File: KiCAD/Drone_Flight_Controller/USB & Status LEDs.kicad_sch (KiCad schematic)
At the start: 26 parts, among them P601 USB_C_Plug_USB2.0, Q601 BC846C, Q602 BC846C, Q603 BC846C, Q604 BC846C, Q605 BC846C, Q606 BC846C, Q607 BC846C, U601 MCP2200-I-SO, Y601 CSTNE12M0GH5L000R0

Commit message: Change footprints to HandSoldering
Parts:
- D601: footprint Diode_SMD:D_SOD-323F -> Diode_SMD:D_SOD-323_HandSoldering
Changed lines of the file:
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@@
 			)
 		)
-		(property "Footprint" "Diode_SMD:D_SOD-323F"
+		(property "Footprint" "Diode_SMD:D_SOD-323_HandSoldering"
 			(at 97.79 45.72 0)
 			(effects

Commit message: add footprint of USB C connector
add footprint of USB C connector
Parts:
- P601: footprint Connector_PinHeader_2.54mm:PinHeader_1x07_P2.54mm_Vertical -> Connector_USB:USB_C_Receptacle_HRO_TYPE-C-31-M-12
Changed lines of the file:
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@@
 			)
 		)
-		(property "Footprint" "Connector_PinHeader_2.54mm:PinHeader_1x07_P2.54mm_Vertical"
+		(property "Footprint" "Connector_USB:USB_C_Receptacle_HRO_TYPE-C-31-M-12"
 			(at 80.01 60.96 0)
 			(effects

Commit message: part placement and routing
part placement and routing
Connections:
- net -BATT is gone; now on net GND: Q603.2 (E), Q604.2 (E), Q605.2 (E)
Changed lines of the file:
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@@
-	)
-	(symbol
-		(lib_id "power:-BATT")
-		(at 218.44 157.48 180)
-		(unit 1)
-		(exclude_from_sim no)
-		(in_bom yes)
-		(on_board yes)
-		(dnp no)
-		(fields_autoplaced yes)
-		(property "Reference" "#PWR0610"
-			(at 218.44 153.67 0)
-			(effects
-				(font
-					(size 1.27 1.27)
-				)
-				(hide yes)
-			)
-		)
-		(property "Value" "-BATT"
-			(at 218.44 162.56 0)
-			(effects
-				(font
-					(size 1.27 1.27)
-				)
-			)
-		)
-		(property "Footprint" ""
-			(at 218.44 157.48 0)
-			(effects
-				(font
-					(size 1.27 1.27)
-				)
-				(hide yes)
-			)
-		)
-		(property "Datasheet" ""
-			(at 218.44 157.48 0)
-			(effects
-				(font
-					(size 1.27 1.27)
-				)
-				(hide yes)
-			)
-		)
-		(property "Description" "Power symbol creates a global label with name \"-BATT\""
-			(at 218.44 157.48 0)
-			(effects
-				(font
-					(size 1.27 1.27)
-				)
-				(hide yes)
-			)
-		)
-		(pin "1"
-		)
-		(instances
-			(project "Drone_Flight_Controller"
-				(path "/05daaa24-e506-4b9a-9564-8bf799413ca8/8421779c-d2a0-463b-acfb-bef6fd845f5d"
-					(reference "#PWR0610")
-					(unit 1)
-				)
-			)
-		)
 	)
 	(symbol
@@
 					(unit 1)
 				)
+			)
+		)
+	)
+	(symbol
+		(lib_id "power:GND")
+		(at 218.44 157.48 0)
+		(unit 1)
+		(exclude_from_sim no)
+		(in_bom yes)
+		(on_board yes)
+		(dnp no)
+		(fields_autoplaced yes)
+		(property "Reference" "#PWR01"
+			(at 218.44 163.83 0)
+			(effects
+				(font
+					(size 1.27 1.27)
+				)
+				(hide yes)
+			)
+		)
+		(property "Value" "GND"
+			(at 218.44 162.56 0)
+			(effects
+				(font
+					(size 1.27 1.27)
+				)
+			)
+		)
+		(property "Footprint" ""
+			(at 218.44 157.48 0)
+			(effects
+				(font
+					(size 1.27 1.27)
+				)
+				(hide yes)
+			)
+		)
+		(property "Datasheet" ""
+			(at 218.44 157.48 0)
+			(effects
+				(font
+					(size 1.27 1.27)
+				)
+				(hide yes)
+			)
+		)
+		(property "Description" "Power symbol creates a global label with name \"GND\" , ground"
+			(at 218.44 157.48 0)
+			(effects
+				(font
+					(size 1.27 1.27)
+				)
+				(hide yes)
+			)
+		)
+		(pin "1"
+		)
+		(instances
+			(project "Drone_Flight_Controller"
+				(path "/05daaa24-e506-4b9a-9564-8bf799413ca8/8421779c-d2a0-463b-acfb-bef6fd845f5d"
+					(reference "#PWR01")
+					(unit 1)
+				)

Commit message: Fix errors
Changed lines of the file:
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@@
 	(title_block
 		(title "USB & Status LEDs")
-		(date "2025-09-19")
+		(date "2025-09-21")
 		(rev "V2")
 		(company "HTL Steyr")
@@
 	)
 	(junction
-		(at 109.22 45.72)
-		(diameter 0)
-		(color 0 0 0 0)
-	)
-	(junction
 		(at 228.6 50.8)
 		(diameter 0)
@@
 	)
 	(junction
-		(at 156.21 45.72)
-		(diameter 0)
-		(color 0 0 0 0)
-	)
-	(junction
 		(at 76.2 86.36)
 		(diameter 0)
@@
 	(wire
 		(pts
-			(xy 118.11 43.18) (xy 118.11 45.72)
-		)
-		(stroke
-			(width 0)
-			(type default)
-		)
-	)
-	(wire
-		(pts
 			(xy 166.37 78.74) (xy 166.37 96.52)
 		)
@@
 	(wire
 		(pts
-			(xy 118.11 45.72) (xy 109.22 45.72)
-		)
-		(stroke
-			(width 0)
-			(type default)
-		)
-	)
-	(wire
-		(pts
 			(xy 198.12 154.94) (xy 198.12 157.48)
 		)
@@
 	(wire
 		(pts
-			(xy 156.21 43.18) (xy 156.21 45.72)
-		)
-		(stroke
-			(width 0)
-			(type default)
-		)
-	)
-	(wire
-		(pts
 			(xy 208.28 50.8) (xy 198.12 50.8)
 		)
@@
 	)
 	(symbol
-		(lib_id "power:PWR_FLAG")
-		(at 156.21 43.18 0)
-		(unit 1)
-		(exclude_from_sim no)
-		(in_bom yes)
-		(on_board yes)
-		(dnp no)
-		(fields_autoplaced yes)
-		(property "Reference" "#FLG0602"
-			(at 156.21 41.275 0)
-			(effects
-				(font
-					(size 1.27 1.27)
-				)
-				(hide yes)
-			)
-		)
-		(property "Value" "PWR_FLAG"
-			(at 156.21 38.1 0)
-			(effects
-				(font
-					(size 1.27 1.27)
-				)
-			)
-		)
-		(property "Footprint" ""
-			(at 156.21 43.18 0)
-			(effects
-				(font
-					(size 1.27 1.27)
-				)
-				(hide yes)
-			)
-		)
-		(property "Datasheet" "~"
-			(at 156.21 43.18 0)
-			(effects
-				(font
-					(size 1.27 1.27)
-				)
-				(hide yes)
-			)
-		)
-		(property "Description" "Special symbol for telling ERC where power comes from"
-			(at 156.21 43.18 0)
-			(effects
-				(font
-					(size 1.27 1.27)
-				)
-				(hide yes)
-			)
-		)
-		(pin "1"
-		)
-		(instances
-			(project ""
-				(path "/05daaa24-e506-4b9a-9564-8bf799413ca8/8421779c-d2a0-463b-acfb-bef6fd845f5d"
-					(reference "#FLG0602")
-					(unit 1)
-				)
-			)
-		)
-	)
-	(symbol
 		(lib_id "power:+5V")
 		(at 248.92 48.26 0)
@@
 					(unit 1)
 				)
-			)
-		)
-	)
-	(symbol
-		(lib_id "power:PWR_FLAG")
-		(at 118.11 43.18 0)
-		(unit 1)
-		(exclude_from_sim no)
-		(in_bom yes)
-		(on_board yes)
-		(dnp no)
-		(fields_autoplaced yes)
-		(property "Reference" "#FLG0601"
-			(at 118.11 41.275 0)
-			(effects
-				(font
-					(size 1.27 1.27)
-				)
-				(hide yes)
-			)
-		)
-		(property "Value" "PWR_FLAG"
-			(at 118.11 38.1 0)
-			(effects
-				(font
-					(size 1.27 1.27)
-				)
-			)
-		)
-		(property "Footprint" ""
-			(at 118.11 43.18 0)
-			(effects
-				(font
-					(size 1.27 1.27)
-				)
-				(hide yes)
-			)
-		)
-		(property "Datasheet" "~"
-			(at 118.11 43.18 0)
-			(effects
-				(font
-					(size 1.27 1.27)
-				)
-				(hide yes)
-			)
-		)
-		(property "Description" "Special symbol for telling ERC where power comes from"
-			(at 118.11 43.18 0)
-			(effects
-				(font
-					(size 1.27 1.27)
-				)
-				(hide yes)
-			)
-		)
-		(pin "1"
-		)
-		(instances
-			(project "Drone_Flight_Controller"
-				(path "/05daaa24-e506-4b9a-9564-8bf799413ca8/8421779c-d2a0-463b-acfb-bef6fd845f5d"
-					(reference "#FLG0601")
-					(unit 1)
-				)

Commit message: Fix USB-C Symbol
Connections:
- net at P601.A7 (D-), U601.18 (D-): now also P601.B7 (D-)
- net at P601.A6 (D+), U601.19 (D+): now also P601.B6 (D+)
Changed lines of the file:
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@@
 		(pin "A5"
+		)
+		(pin "B6"
+		)
+		(pin "B7"
 		)
 		(instances

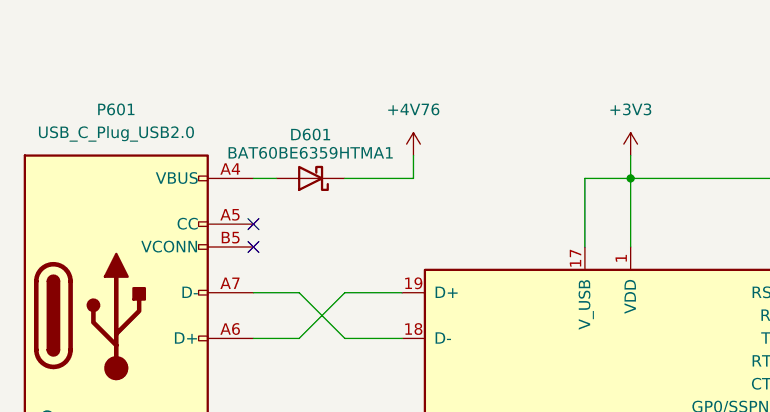
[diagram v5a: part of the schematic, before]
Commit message: Add TVS Diodes to 5V
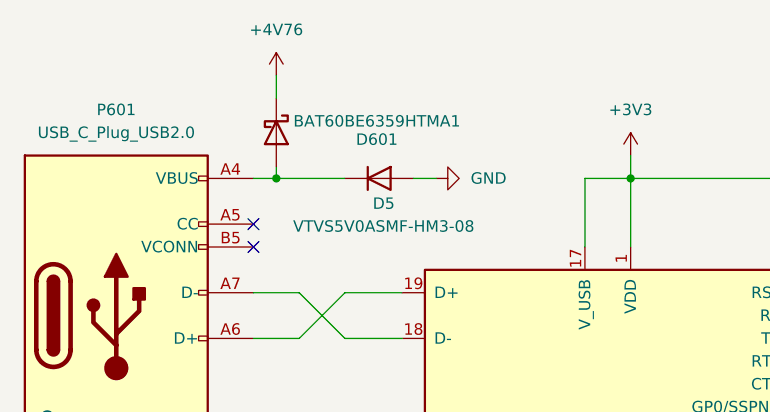
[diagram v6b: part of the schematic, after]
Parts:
- added D5: VTVS5V0ASMF-HM3-08, Diode_SMD:D_SMF, symbol Device:D
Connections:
- net GND: now also D5.2 (A)
- net at D601.2 (A), P601.A4 (VBUS), P601.A9 (VBUS)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: now also D5.1 (K)
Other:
- moved on the sheet: D601
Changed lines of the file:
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@@
 	)
 	(junction
+		(at 93.98 45.72)
+		(diameter 0)
+		(color 0 0 0 0)
+	)
+	(junction
 		(at 228.6 154.94)
 		(diameter 0)
@@
 	(wire
 		(pts
-			(xy 91.44 45.72) (xy 93.98 45.72)
-		)
-		(stroke
-			(width 0)
-			(type default)
-		)
-	)
-	(wire
-		(pts
 			(xy 180.34 134.62) (xy 158.75 134.62)
 		)
@@
 	(wire
 		(pts
+			(xy 93.98 34.29) (xy 93.98 36.83)
+		)
+		(stroke
+			(width 0)
+			(type default)
+		)
+	)
+	(wire
+		(pts
 			(xy 218.44 101.6) (xy 218.44 154.94)
 		)
@@
 	(wire
 		(pts
+			(xy 91.44 45.72) (xy 93.98 45.72)
+		)
+		(stroke
+			(width 0)
+			(type default)
+		)
+	)
+	(wire
+		(pts
 			(xy 158.75 86.36) (xy 153.67 86.36)
 		)
@@
 	(wire
 		(pts
-			(xy 109.22 43.18) (xy 109.22 45.72)
+			(xy 176.53 83.82) (xy 180.34 83.82)
 		)
 		(stroke
@@
 	(wire
 		(pts
-			(xy 176.53 83.82) (xy 180.34 83.82)
+			(xy 93.98 45.72) (xy 101.6 45.72)
 		)
 		(stroke
@@
 	(wire
 		(pts
+			(xy 93.98 45.72) (xy 93.98 44.45)
+		)
+		(stroke
+			(width 0)
+			(type default)
+		)
+	)
+	(wire
+		(pts
 			(xy 187.96 147.32) (xy 251.46 147.32)
 		)
@@
 	(wire
 		(pts
-			(xy 109.22 45.72) (xy 101.6 45.72)
+			(xy 109.22 45.72) (xy 111.76 45.72)
 		)
 		(stroke
@@
 	(symbol
 		(lib_id "power:+5V")
-		(at 109.22 43.18 0)
+		(at 93.98 34.29 0)
 		(unit 1)
 		(exclude_from_sim no)
@@
 		(fields_autoplaced yes)
 		(property "Reference" "#PWR0601"
-			(at 109.22 46.99 0)
+			(at 93.98 38.1 0)
 			(effects
 				(font
@@
 		)
 		(property "Value" "+4V76"
-			(at 109.22 38.1 0)
+			(at 93.98 29.21 0)
 			(effects
 				(font
@@
 		)
 		(property "Footprint" ""
-			(at 109.22 43.18 0)
+			(at 93.98 34.29 0)
 			(effects
 				(font
@@
 		)
 		(property "Datasheet" ""
-			(at 109.22 43.18 0)
+			(at 93.98 34.29 0)
 			(effects
 				(font
@@
 		)
 		(property "Description" "Power symbol creates a global label with name \"+5V\""
-			(at 109.22 43.18 0)
+			(at 93.98 34.29 0)
 			(effects
 				(font
@@
 	)
 	(symbol
+		(lib_id "Device:D")
+		(at 105.41 45.72 0)
+		(unit 1)
+		(exclude_from_sim no)
+		(in_bom yes)
+		(on_board yes)
+		(dnp no)
+		(property "Reference" "D5"
+			(at 105.918 48.514 0)
+			(effects
+				(font
+					(size 1.27 1.27)
+				)
+			)
+		)
+		(property "Value" "VTVS5V0ASMF-HM3-08"
+			(at 105.918 51.054 0)
+			(effects
+				(font
+					(size 1.27 1.27)
+				)
+			)
+		)
+		(property "Footprint" "Diode_SMD:D_SMF"
+			(at 105.41 45.72 0)
+			(effects
+				(font
+					(size 1.27 1.27)
+				)
+				(hide yes)
+			)
+		)
+		(property "Datasheet" "https://www.vishay.com/doc?85891"
+			(at 105.41 45.72 0)
+			(effects
+				(font
+					(size 1.27 1.27)
+				)
+				(hide yes)
+			)
+		)
+		(property "Description" "Diode"
+			(at 105.41 45.72 0)
+			(effects
+				(font
+					(size 1.27 1.27)
+				)
+				(hide yes)
+			)
+		)
+		(property "Sim.Device" "D"
+			(at 105.41 45.72 0)
+			(effects
+				(font
+					(size 1.27 1.27)
+				)
+				(hide yes)
+			)
+		)
+		(property "Sim.Pins" "1=K 2=A"
+			(at 105.41 45.72 0)
+			(effects
+				(font
+					(size 1.27 1.27)
+				)
+				(hide yes)
+			)
+		)
+		(property "Link" "https://www.mouser.at/ProductDetail/Vishay-General-Semiconductor/VTVS5V0ASMF-HM3-08?qs=VPy2d4TTPFGNex1IuahNkg%3D%3D"
+			(at 105.41 45.72 90)
+			(effects
+				(font
+					(size 1.27 1.27)
+				)
+				(hide yes)
+			)
+		)
+		(pin "2"
+		)
+		(pin "1"
+		)
+		(instances
+			(project "Drone_Flight_Controller"
+				(path "/05daaa24-e506-4b9a-9564-8bf799413ca8/8421779c-d2a0-463b-acfb-bef6fd845f5d"
+					(reference "D5")
+					(unit 1)
+				)
+			)
+		)
+	)
+	(symbol
 		(lib_id "power:GND")
 		(at 248.92 157.48 0)
@@
 	(symbol
 		(lib_id "Device:D_Schottky")
-		(at 97.79 45.72 180)
+		(at 93.98 40.64 270)
 		(unit 1)
 		(exclude_from_sim no)
@@
 		(dnp no)
 		(property "Reference" "D601"
-			(at 97.79 40.894 0)
+			(at 105.156 41.402 90)
 			(effects
 				(font
@@
 		)
 		(property "Value" "BAT60BE6359HTMA1"
-			(at 97.79 42.926 0)
+			(at 105.156 39.37 90)
 			(effects
 				(font
@@
 		)
 		(property "Footprint" "Diode_SMD:D_SOD-323_HandSoldering"
-			(at 97.79 45.72 0)
+			(at 93.98 40.64 0)
 			(effects
 				(font
@@
 		)
 		(property "Datasheet" "https://www.mouser.at/datasheet/3/70/1/Infineon-BAT60BSERIES-DS-v01_01-en.pdf"
-			(at 97.79 45.72 0)
+			(at 93.98 40.64 0)
 			(effects
 				(font
@@
 		)
 		(property "Description" "Schottky diode"
-			(at 97.79 45.72 0)
+			(at 93.98 40.64 0)
 			(effects
 				(font
@@
 		)
 		(property "Link" "https://www.mouser.at/ProductDetail/Infineon-Technologies/BAT60BE6359HTMA1?qs=znymxvEW7YnVGCVVXuqMnw%3D%3D"
-			(at 97.79 45.72 0)
+			(at 93.98 40.64 0)
 			(effects
 				(font
@@
 					(unit 1)
 				)
+			)
+		)
+	)
+	(symbol
+		(lib_id "power:GND")
+		(at 111.76 45.72 90)
+		(unit 1)
+		(exclude_from_sim no)
+		(in_bom yes)
+		(on_board yes)
+		(dnp no)
+		(fields_autoplaced yes)
+		(property "Reference" "#PWR04"
+			(at 118.11 45.72 0)
+			(effects
+				(font
+					(size 1.27 1.27)
+				)
+				(hide yes)
+			)
+		)
+		(property "Value" "GND"
+			(at 115.57 45.7199 90)
+			(effects
+				(font
+					(size 1.27 1.27)
+				)
+				(justify right)
+			)
+		)
+		(property "Footprint" ""
+			(at 111.76 45.72 0)
+			(effects
+				(font
+					(size 1.27 1.27)
+				)
+				(hide yes)
+			)
+		)
+		(property "Datasheet" ""
+			(at 111.76 45.72 0)
+			(effects
+				(font
+					(size 1.27 1.27)
+				)
+				(hide yes)
+			)
+		)
+		(property "Description" "Power symbol creates a global label with name \"GND\" , ground"
+			(at 111.76 45.72 0)
+			(effects
+				(font
+					(size 1.27 1.27)
+				)
+				(hide yes)
+			)
+		)
+		(pin "1"
+		)
+		(instances
+			(project ""
+				(path "/05daaa24-e506-4b9a-9564-8bf799413ca8/8421779c-d2a0-463b-acfb-bef6fd845f5d"
+					(reference "#PWR04")
+					(unit 1)
+				)

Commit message: Cleanup & Re-annotate
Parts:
- renumbered D601 to D701, D5 to D702, D602 to D703, D603 to D704, D604 to D705, D605 to D706, D606 to D707, D607 to D708, D608 to D709, P601 to P701, Q601 to Q701, Q602 to Q702, Q603 to Q703, Q604 to Q704, Q605 to Q705, Q606 to Q706, Q607 to Q707, R601 to R701, R602 to R702, R603 to R703, R604 to R704, R605 to R705, R606 to R706, R607 to R707, R608 to R708, U601 to U701, Y601 to Y701

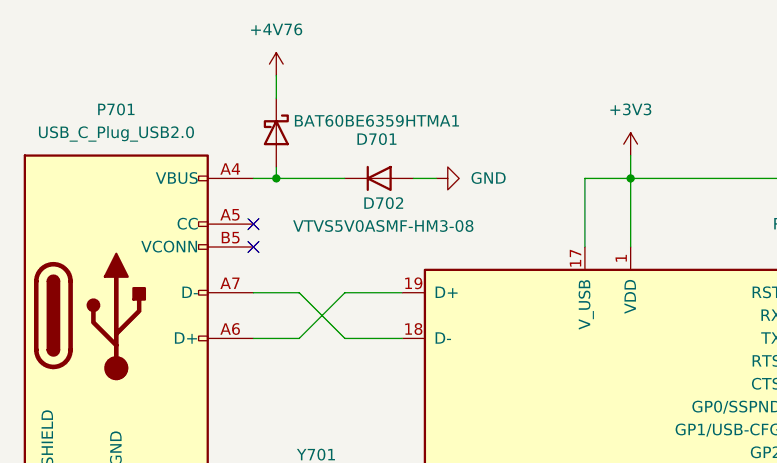
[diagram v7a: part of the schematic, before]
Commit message: add USB C resistors
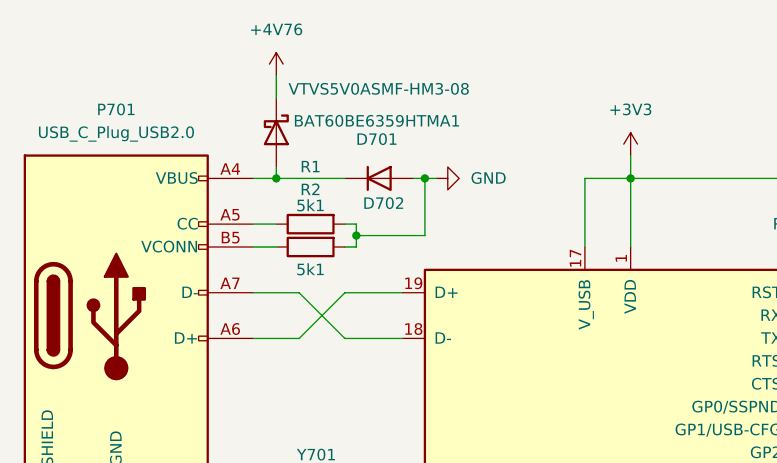
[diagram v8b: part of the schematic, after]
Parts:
- added R1, R2: 5k1, Resistor_SMD:R_0805_2012Metric_Pad1.20x1.40mm_HandSolder, symbol Device:R
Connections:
- net GND: now also R1.2, R2.2
- net at P701.A5 (CC): now also R1.1
- net at P701.B5 (VCONN): now also R2.1
- no-connect marks 2 -> 0
